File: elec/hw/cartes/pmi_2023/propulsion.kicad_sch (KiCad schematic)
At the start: 45 parts, among them U1 DRV8231ADDAR, U2 DRV8231ADDAR, U3 EESX1321, U4 EESX1321

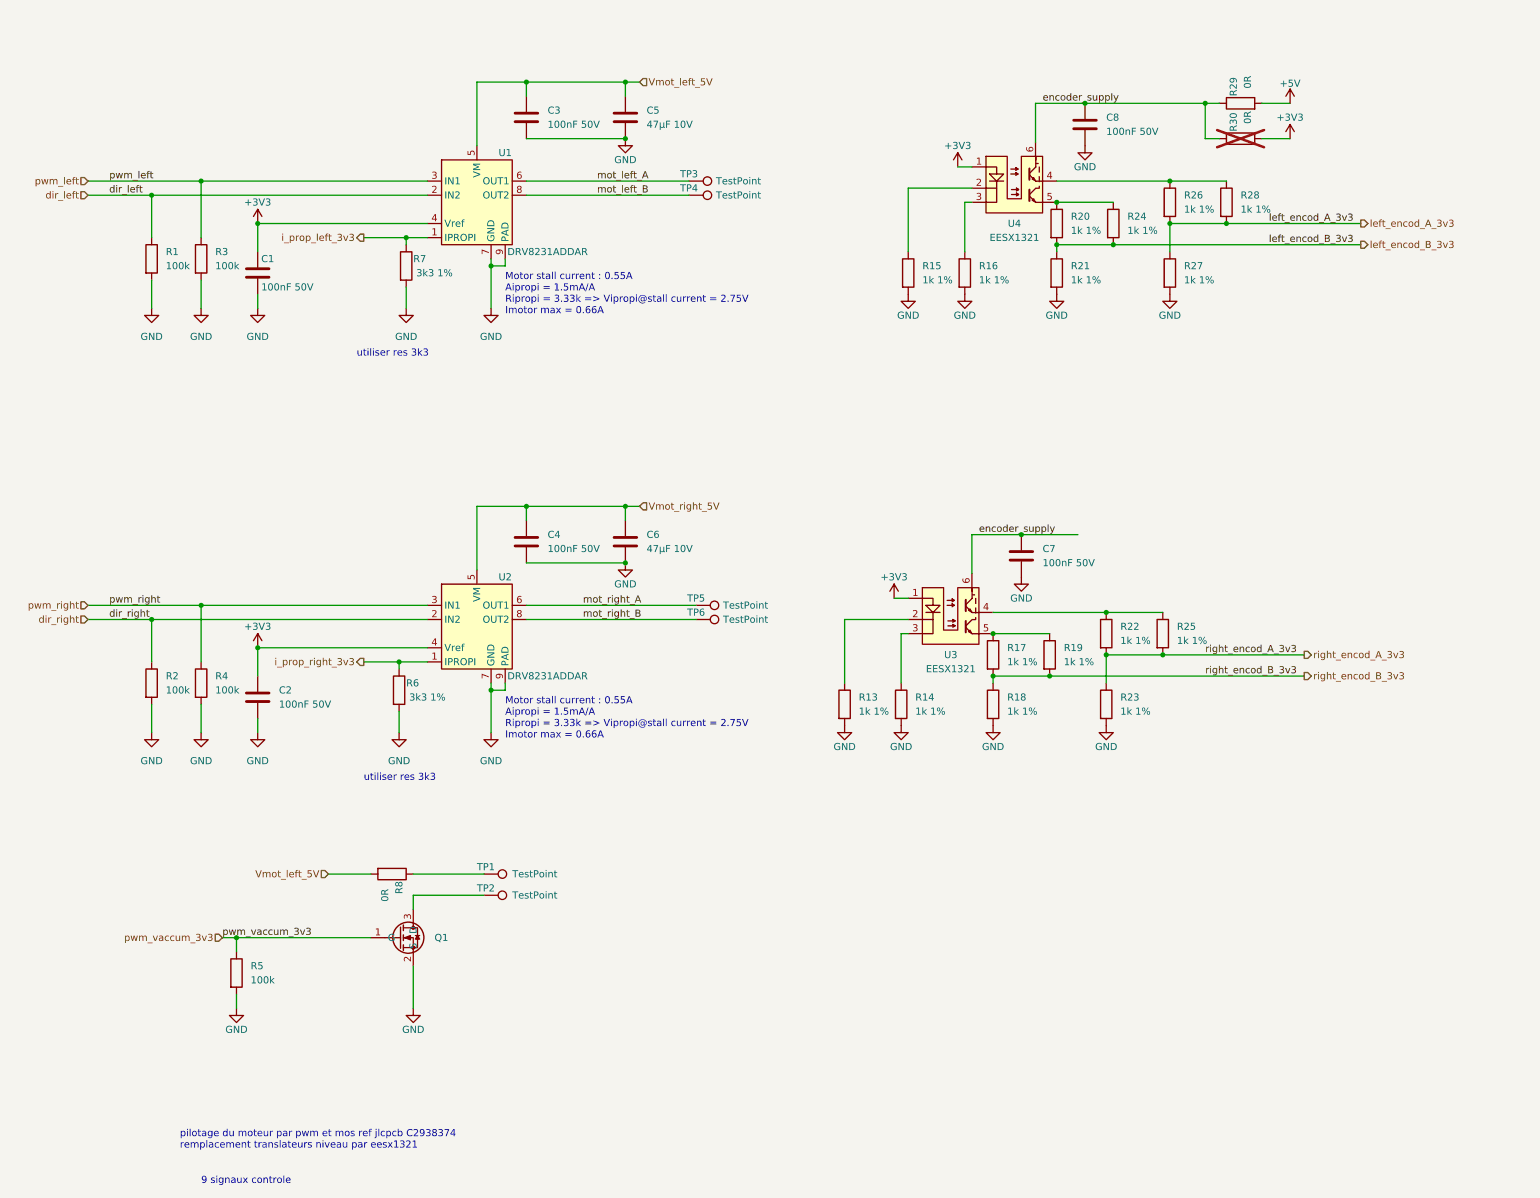
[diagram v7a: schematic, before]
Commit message: added oled display power supply res selectors, jlcpcb refs : wip
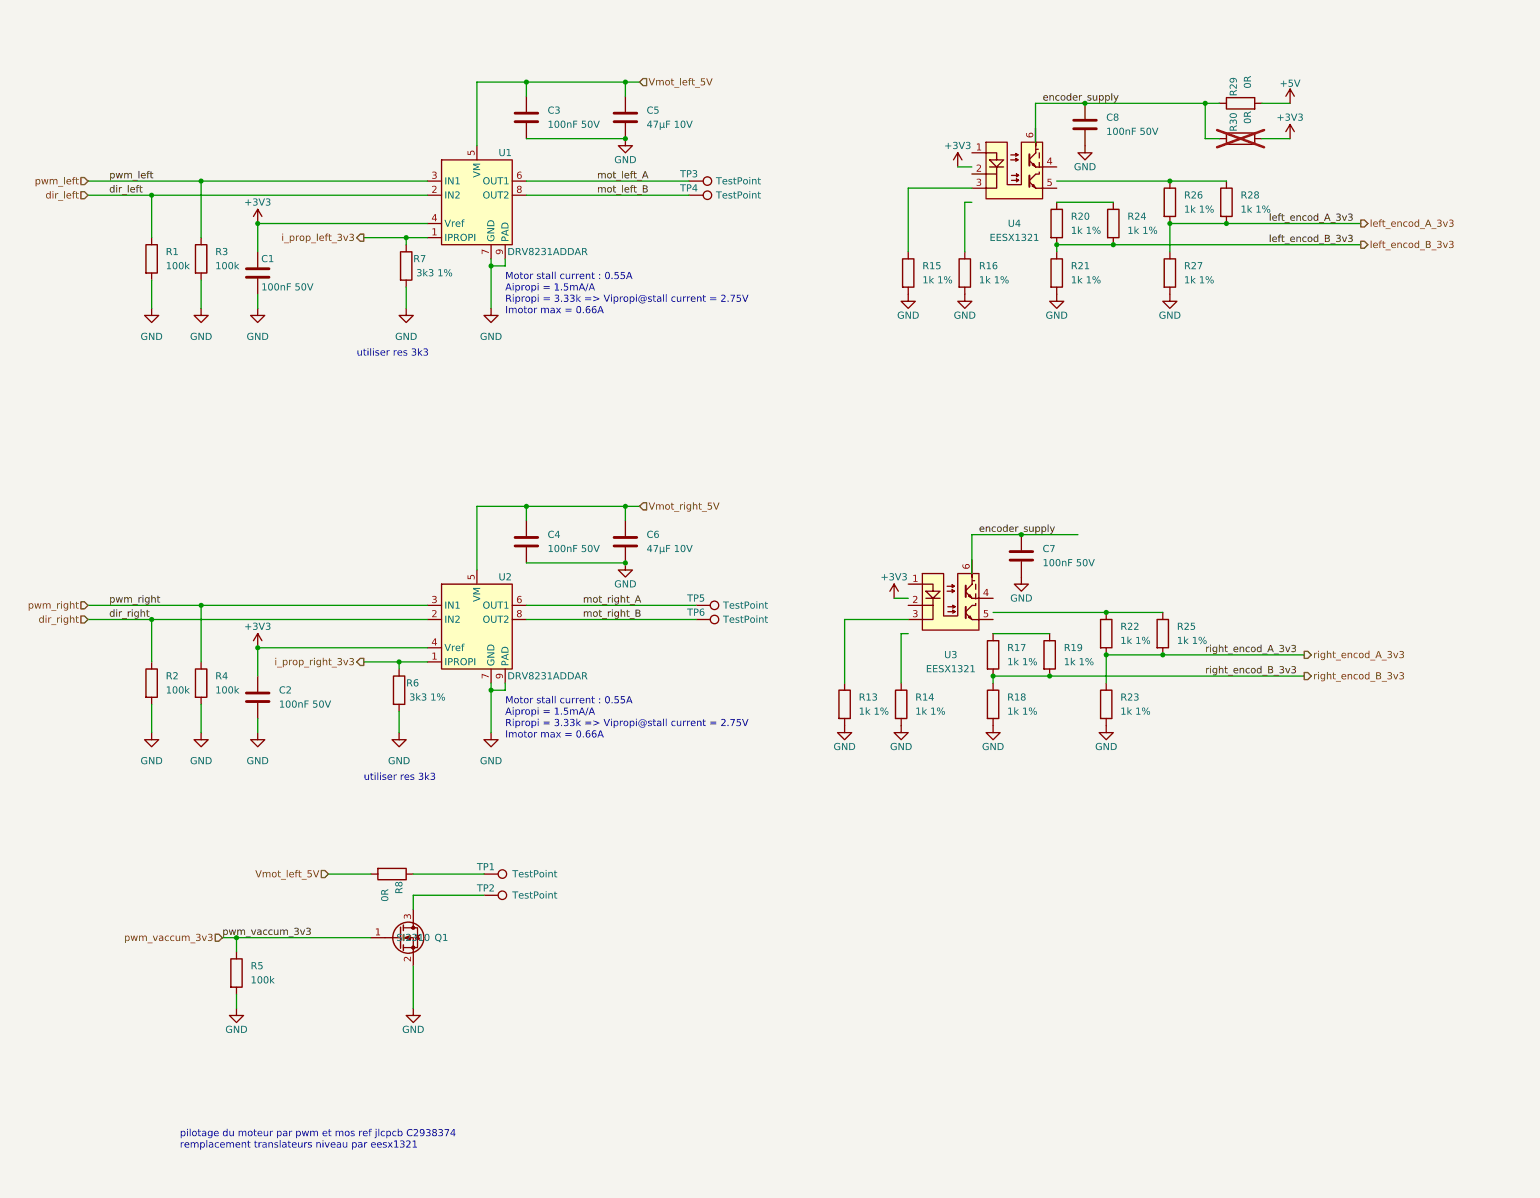
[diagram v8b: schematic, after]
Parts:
- Q1: value ~ -> SI2310
- R6, R7: JLCPCB (none) -> C22978
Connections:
- net +3V3: no longer U3.1 (A), U4.1 (A)
- net encoder_supply: no longer U3.6 (C), U4.6 (C)
- net at R14.1: no longer U3.3 (C2)
- net at R22.1, R25.1: no longer U3.4 (E1)
- net at R17.1, R19.1: no longer U3.5 (E2)
- net at R26.1, R28.1: no longer U4.4 (E1)
- net at R20.1, R24.1: no longer U4.5 (E2)
- net at U3.2 (C1): no longer R13.1
- net at U4.2 (C1): no longer R15.1
- net at U4.3 (C2): now also R15.1; no longer R16.1
- new net: R13.1, U3.3 (C2)
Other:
- note removed: "9 signaux controle"
- moved on the sheet: U3, U4
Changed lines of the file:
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@@
 	)
 	(junction
-		(at 187.96 123.19)
-		(diameter 0)
-		(color 0 0 0 0)
-	)
-	(junction
 		(at 226.06 27.94)
 		(diameter 0)
@@
 	)
 	(junction
-		(at 199.39 45.72)
-		(diameter 0)
-		(color 0 0 0 0)
-	)
-	(junction
 		(at 121.92 34.29)
 		(diameter 0)
@@
 		)
 	)
-	(text "9 signaux controle"
-		(exclude_from_sim no)
-		(at 45.72 222.25 0)
-		(effects
-			(font
-				(size 1.27 1.27)
-			)
-			(justify left bottom)
-		)
-	)
 	(text "Motor stall current : 0.55A\nAipropi = 1.5mA/A\nRipropi = 3.33k => Vipropi@stall current = 2.75V\nImotor max = 0.66A"
 		(exclude_from_sim no)
@@
 			)
 		)
-		(property "Description" "Unpolarized capacitor"
+		(property "Description" "Unpolarized capacitor tol +/-10%"
 			(at 55.88 58.42 0)
 			(effects
@@
 			)
 		)
-		(property "Description" "Unpolarized capacitor"
+		(property "Description" "Unpolarized capacitor tol +/-10%"
 			(at 104.14 30.48 0)
 			(effects
@@
 			)
 		)
-		(property "Value" "~"
+		(property "Value" "SI2310"
 			(at 83.82 177.8 0)
 			(effects
@@
 			)
 		)
-		(property "Description" "Unpolarized capacitor"
+		(property "Description" "Unpolarized capacitor tol +/-10%"
 			(at 55.88 134.62 0)
 			(effects
@@
 			)
 		)
-		(property "Description" ""
+		(property "Description" "Unpolarized capacitor"
 			(at 121.92 30.48 0)
 			(effects
@@
 			)
 		)
-		(property "Description" "Unpolarized capacitor"
+		(property "Description" "Unpolarized capacitor tol +/-10%"
 			(at 204.47 31.75 0)
 			(effects
@@
 			)
 		)
-		(property "Description" ""
+		(property "Description" "Resistor"
 			(at 81.28 133.35 0)
 			(effects
@@
 			)
 		)
-		(property "JLCPCB" ""
+		(property "JLCPCB" "C22978"
 			(at 81.28 133.35 0)
 			(effects
@@
 			)
 		)
-		(property "Description" "Unpolarized capacitor"
+		(property "Description" "Unpolarized capacitor tol +/-10%"
 			(at 193.04 109.22 0)
 			(effects
@@
 			)
 		)
-		(property "Description" ""
+		(property "Description" "Unpolarized capacitor"
 			(at 121.92 106.68 0)
 			(effects
@@
 			)
 		)
-		(property "Description" "Unpolarized capacitor"
+		(property "Description" "Unpolarized capacitor tol +/-10%"
 			(at 104.14 106.68 0)
 			(effects
@@
 			)
 		)
-		(property "Description" ""
+		(property "Description" "Resistor"
 			(at 82.55 57.15 0)
 			(effects
@@
 			)
 		)
-		(property "JLCPCB" ""
+		(property "JLCPCB" "C22978"
 			(at 82.55 57.15 0)
 			(effects
